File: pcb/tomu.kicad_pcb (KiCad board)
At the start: 2 copper layers, 13 x 9.4 mm, 17 parts, among them P3 USB-PCB, U1 EFM32HG309

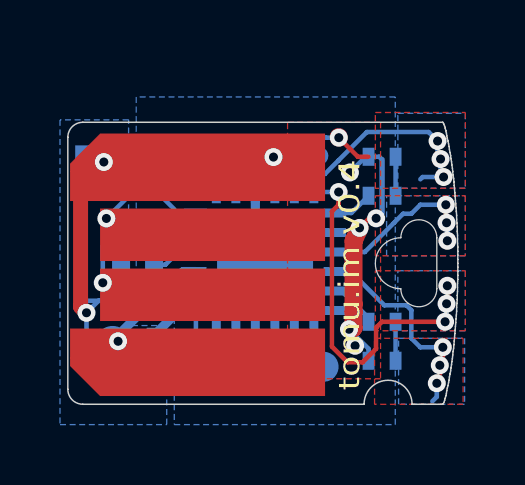
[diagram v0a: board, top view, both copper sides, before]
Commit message: v0.4Z: width 1cm, led 0603
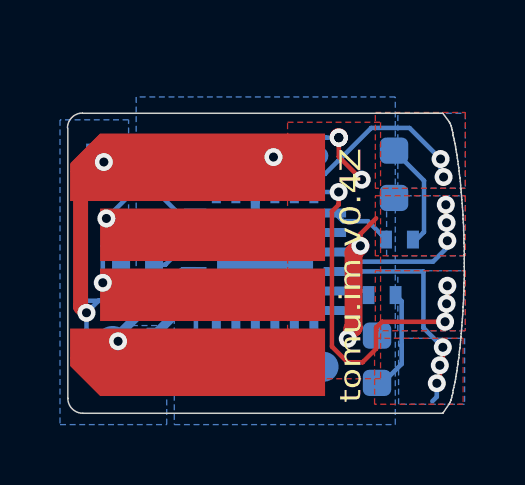
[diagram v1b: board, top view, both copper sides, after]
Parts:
- removed XX1: Button solder mask removal, usb-pcb:soldermask-removal
- D1: value LED Green 0402 -> LED Green 0603; footprint LEDs:LED_0402 -> LED_SMD:LED_0603_1608Metric
- D2: value LED, Red, 0402 -> LED, Red, 0603; footprint LEDs:LED_0402 -> LED_SMD:LED_0603_1608Metric
- P1: renamed from Serial headers; footprint pads-1x3-slim -> usb-pcb:pads-1x3-slim
- P2: renamed from SWD headers; footprint pads-1x3 -> usb-pcb:pads-1x3
- P3: footprint USB-PCB -> usb-pcb:USB-PCB
- P5: renamed from USB power
- moved R1 1.57 mm to (28.1, 21.0)
- moved P1 1.08 mm to (21.4, 25.3)
- moved R2 0.89 mm to (27.5, 22.9)
- moved D1 0.71 mm to (27.9, 18.8), turned to -90 degrees
- moved P2 0.37 mm to (18.0, 18.2)
- moved D2 0.18 mm to (27.3, 25.0), turned to 90 degrees
- renumbered Reset to P4, 3.3V to P6
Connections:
- net //RESET renamed //RESET
- U1 pad 6: Net-(U1-Pad6) -> unconnected-(U1-Pad6)
- U1 pad 8: Net-(U1-Pad8) -> unconnected-(U1-Pad8)
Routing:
- net +3V3: track 20.7 -> 16.0 mm, vias 6 -> 5
- net Net-(D1-Pad1): track 1.30 -> 3.60 mm
- net Net-(D2-Pad1): track 1.30 -> 3.37 mm
- net /CAP0B: track 8.45 -> 7.25 mm, vias 3 -> 2
- net /CAP1A: track 8.64 -> 9.40 mm
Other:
- board size 13 x 9.4 mm -> 13.2 x 10 mm
- net class Default removed
- board text added: "tomu.im v0.4Z"
- board text removed: "tomu.im v0.4"
